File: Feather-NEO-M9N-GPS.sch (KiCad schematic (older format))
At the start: 42 parts, among them IC1 PRTR5V0U2F,115, J6 USB_B_Micro, U1 NEO-M9N

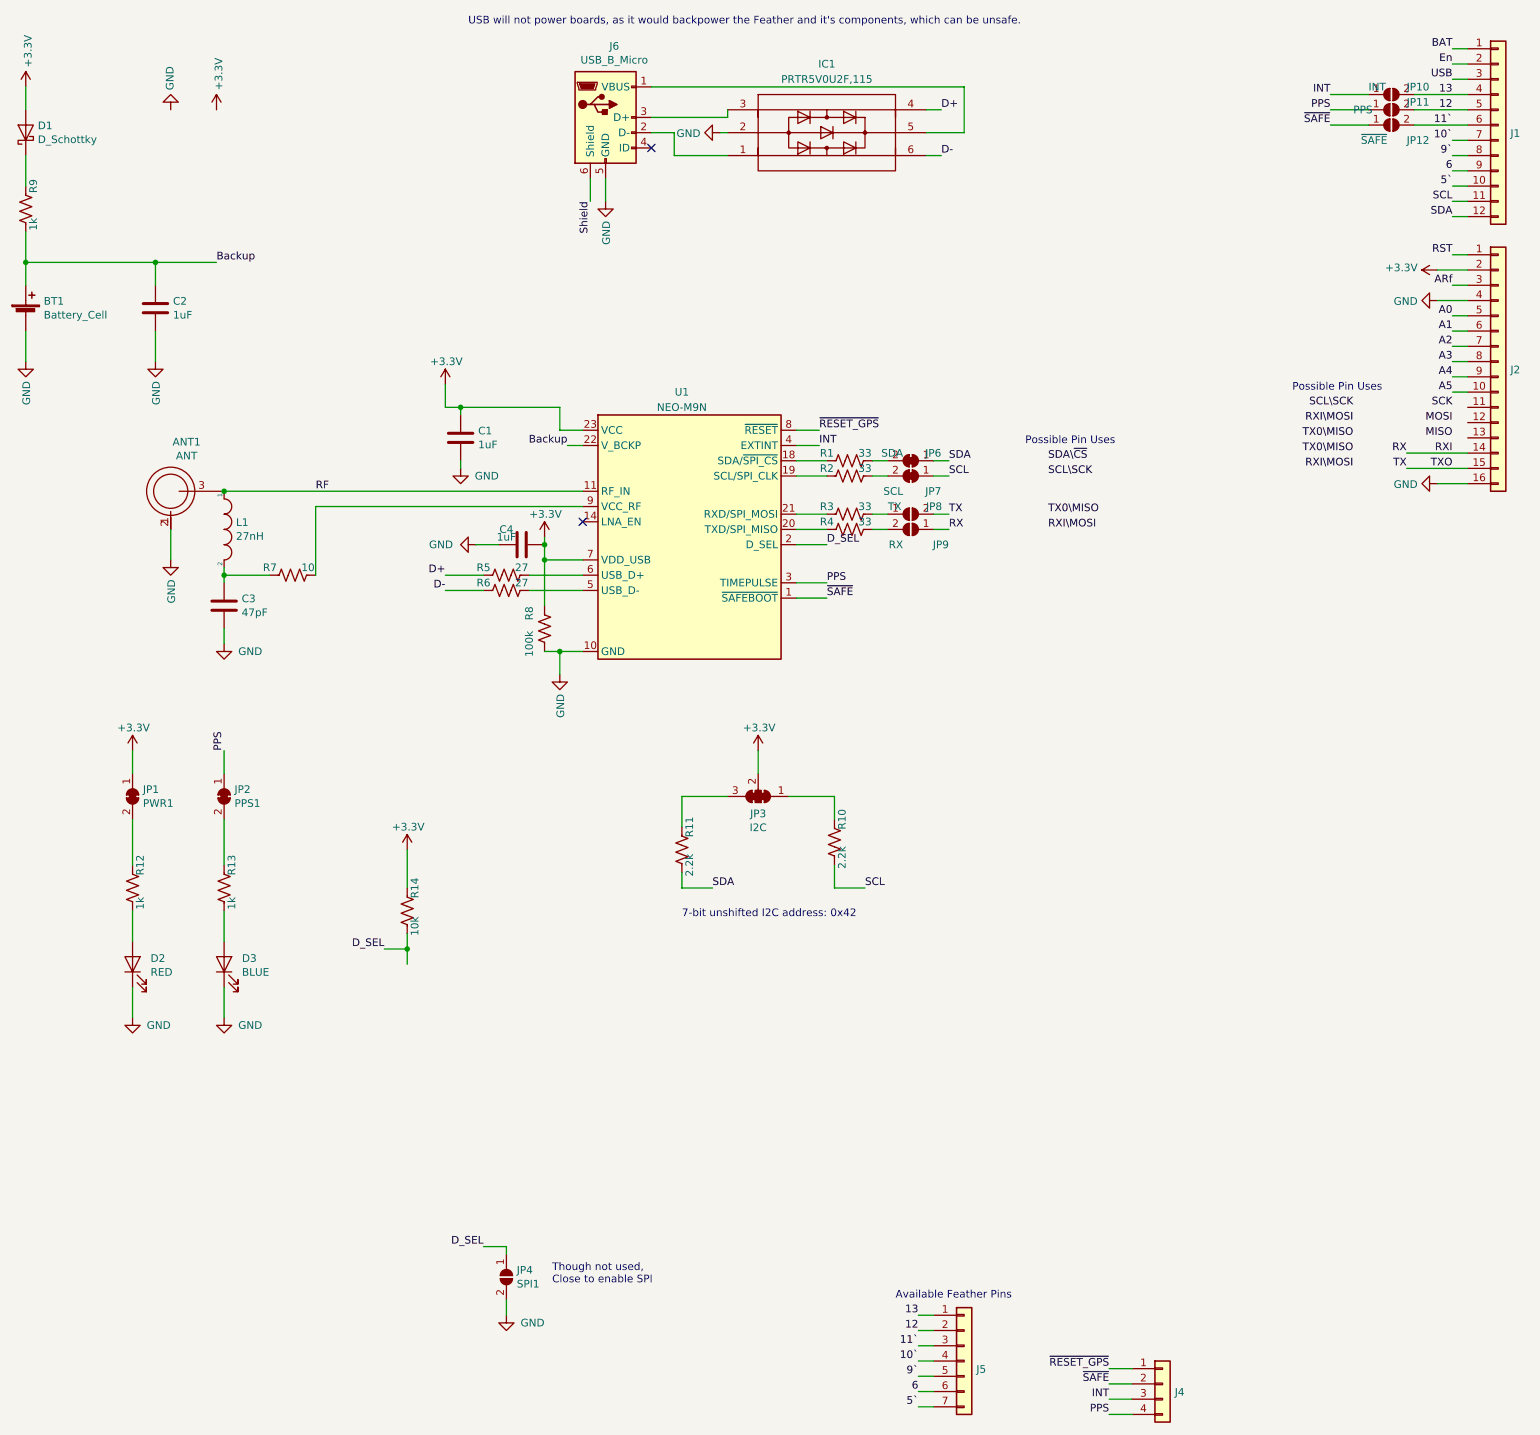
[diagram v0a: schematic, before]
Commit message: Rev2!
Rev2 includes proper USB implementation, some small trace fixes, and power regulation
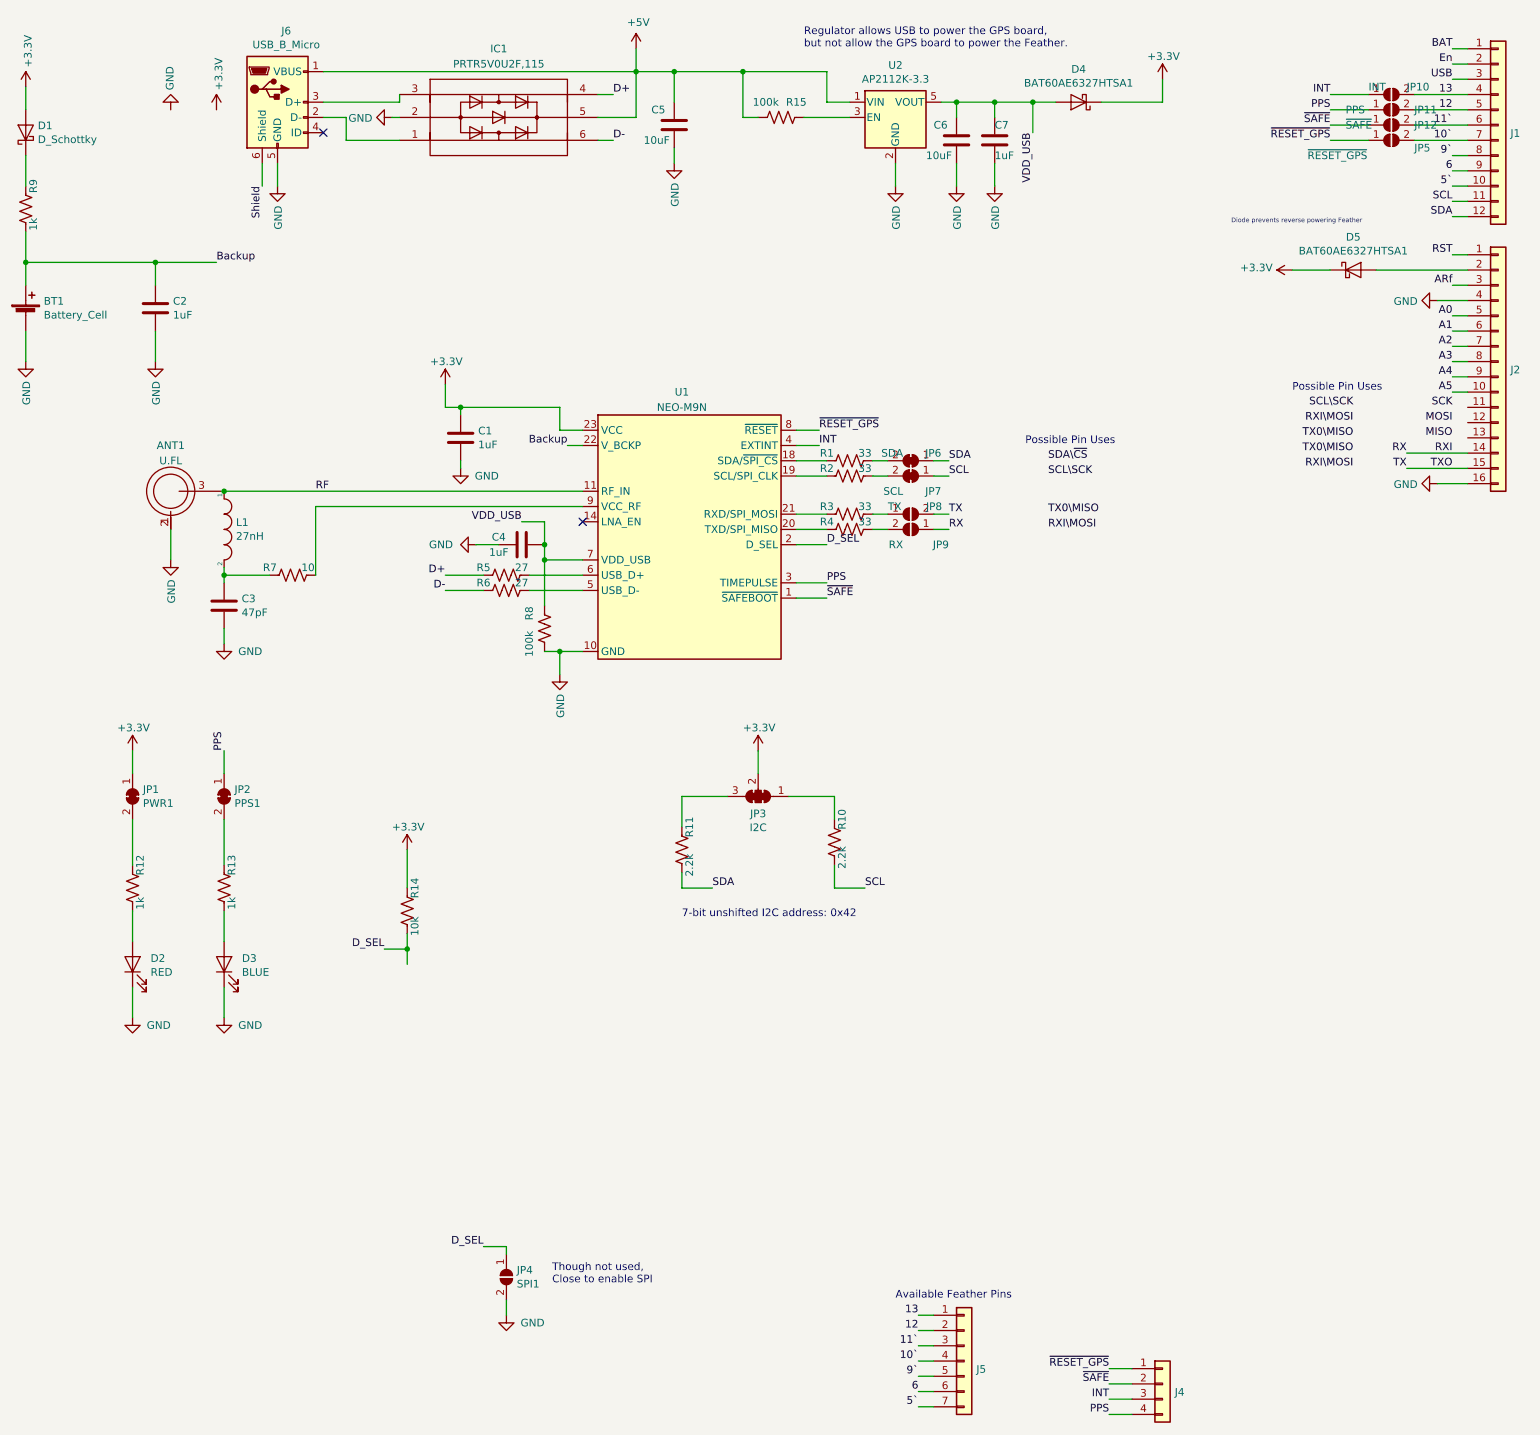
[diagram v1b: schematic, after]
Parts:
- added C5, C6: 10uF, Capacitor_SMD:C_0603_1608Metric, symbol Device:C
- added C7: 1uF, Capacitor_SMD:C_0603_1608Metric, symbol Device:C
- added D4, D5: BAT60AE6327HTSA1, SOD2513X110N, symbol Device:D_Schottky
- added JP5: ~RESET_GPS, Jumper:SolderJumper-2_P1.3mm_Open_RoundedPad1.0x1.5mm, symbol Jumper:SolderJumper_2_Open
- added R15: 100k, Resistor_SMD:R_0603_1608Metric, symbol Device:R_US
- added U2: AP2112K-3.3, Package_TO_SOT_SMD:SOT-23-5, symbol Regulator_Linear:AP2112K-3.3
- ANT1: value ANT -> U.FL
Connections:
- net +3V3: now also D4.1 (K), D5.1 (K); no longer C4.2, J2.2 (Pin_2), R8.2, U1.7 (VDD_USB)
- net 10`: now also JP5.2 (B)
- net GND: now also C5.1, C6.1, C7.1, U2.2 (GND)
- net ~RESET_GPS: now also JP5.1 (A)
- net +5V: now reaches IC1.5, J6.1 (VBUS)
- net +5V: now also C5.2, R15.1, U2.1 (VIN)
- new net: D5.2 (A), J2.2 (Pin_2)
- new net: R15.2, U2.3 (EN)
- new net VDD_USB: C4.2, C6.2, C7.2, D4.2 (A), R8.2, U1.7 (VDD_USB), U2.5 (VOUT)
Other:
- note added: "Diode prevents reverse powering Feather"
- note added: "Regulator allows USB to power the GPS board,\nbut not allow the GPS board to power the Feather."
- note removed: "USB will not power boards, as it would backpower the Feather and it's components, which can be unsafe."
- moved on the sheet: IC1, J6
